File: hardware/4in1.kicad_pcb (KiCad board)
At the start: 6 copper layers, 41.6 x 42.5 mm, 222 parts, among them J1 SM08B-SRSS-TB, Q1 SP40N01GHNK, Q10 SP40N01GHNK, Q11 SP40N01GHNK, Q12 SP40N01GHNK, Q13 SP40N01GHNK, Q14 SP40N01GHNK, Q15 SP40N01GHNK, Q16 SP40N01GHNK, Q17 SP40N01GHNK, Q18 SP40N01GHNK, Q19 SP40N01GHNK, Q2 SP40N01GHNK, Q20 SP40N01GHNK, Q21 SP40N01GHNK, Q22 SP40N01GHNK, Q23 SP40N01GHNK, Q24 SP40N01GHNK, Q3 SP40N01GHNK, Q4 SP40N01GHNK, Q5 SP40N01GHNK, Q6 SP40N01GHNK, Q7 SP40N01GHNK, Q8 SP40N01GHNK, Q9 SP40N01GHNK, U10 NSG2065Q, U12 INA186A3IDCKR, U13 LMR54406DBVR, U14 FTC160808S4R7MBCA, U15 TLV76733DRVR, U2 AT32F421G8U7, U4 NSG2065Q, U5 AT32F421G8U7, U6 NSG2065Q, U7 AT32F421G8U7, U8 NSG2065Q, U9 AT32F421G8U7

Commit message: Rebrand back silkscreen to incutec, 4.7uF bulk caps on board
incutec silkscreen text added by Stan; bulk cap footprint fields
swapped to FH 1206B475K500NT 4.7uF 50V C29823 matching the committed
schematic change.

Co-Authored-By: Claude Fable 5 <noreply@anthropic.com>
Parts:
- C107 (x3), C108 (x3), C13 (x3), C14 (x3), C17, C18, C2 (x2), C26 (x3), C27 (x3), C3 (x2), C30, C43 (x3), C44 (x3), C6, C69, C70, C8, C82 (x3), C83 (x3), C84 (x3), C85 (x3), C9, C96, C97, C98, C99: value 10uF -> 4.7uF

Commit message: Sync silkscreen rev text to REV3.2 (pipeline rev sync)
Co-Authored-By: Claude Fable 5 <noreply@anthropic.com>
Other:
- board text added: "REV3.2"
- board text removed: "REV3.1"
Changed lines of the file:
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@@
 	)
 	(paper "A4")
+	(title_block
+		(rev "rev3.2")
+	)
 	(layers
 		(0 "F.Cu" signal)
@@
 		)
 	)
-	(gr_text "REV3.1"
+	(gr_text "REV3.2"
 		(at 87.12 56.53 0)
 		(layer "B.SilkS")
@@
 			(justify left bottom mirror)
 		)
-		(render_cache "REV3.1" 0
+		(render_cache "REV3.2" 0
 			(polygon
 				(pts
@@
 			(polygon
 				(pts
-					(xy 82.75759 56.224) (xy 83.052477 56.224) (xy 83.052477 54.604706) (xy 82.906297 54.458417) (xy 82.75759 54.458417)
+					(xy 83.059511 56.224) (xy 83.059511 55.441116) (xy 83.051258 55.374893) (xy 83.027065 55.316478)
+					(xy 82.986092 55.263832) (xy 82.933388 55.222921) (xy 82.874205 55.198631) (xy 82.80639 55.190303)
+					(xy 82.616357 55.190303) (xy 82.616357 54.753523) (xy 82.764624 54.753523) (xy 82.764624 55.043024)
+					(xy 83.059511 55.043024) (xy 83.059511 54.70934) (xy 83.051224 54.642106) (xy 83.027049 54.583432)
+					(xy 82.986311 54.531177) (xy 82.933733 54.490723) (xy 82.87462 54.46667) (xy 82.80683 54.458417)
+					(xy 82.574262 54.458417) (xy 82.50812 54.466599) (xy 82.449388 54.490636) (xy 82.396099 54.531397)
+					(xy 82.354516 54.583896) (xy 82.329898 54.642746) (xy 82.32147 54.710109) (xy 82.32147 55.236245)
+					(xy 82.329839 55.301929) (xy 82.354422 55.359974) (xy 82.396209 55.412429) (xy 82.44957 55.453182)
+					(xy 82.508411 55.477224) (xy 82.574701 55.485409) (xy 82.764624 55.485409) (xy 82.764624 55.928893)
+					(xy 82.616357 55.928893) (xy 82.616357 55.634886) (xy 82.32147 55.634886) (xy 82.32147 56.224)
 				)
 			)

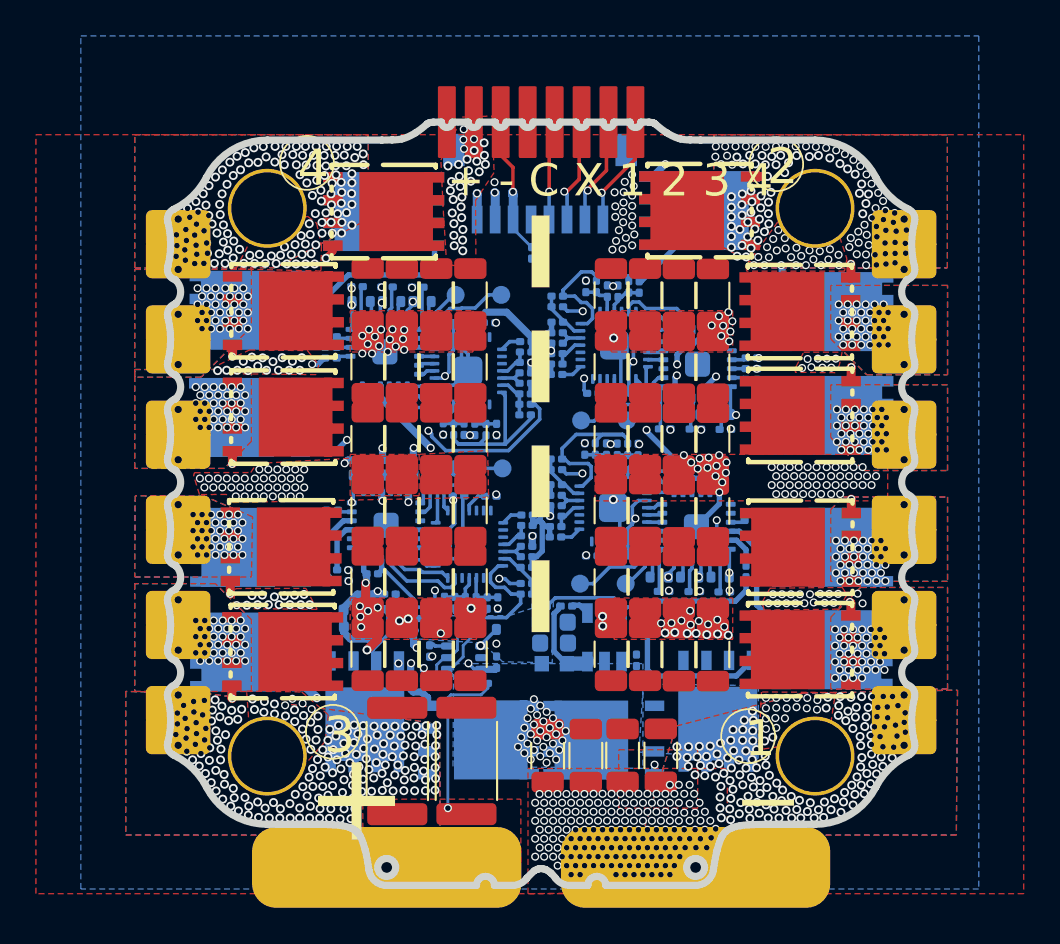
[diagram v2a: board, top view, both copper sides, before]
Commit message: Rebrand silkscreen to incutec, final rev3.3 pass (Stan)
Co-Authored-By: Claude Fable 5 <noreply@anthropic.com>
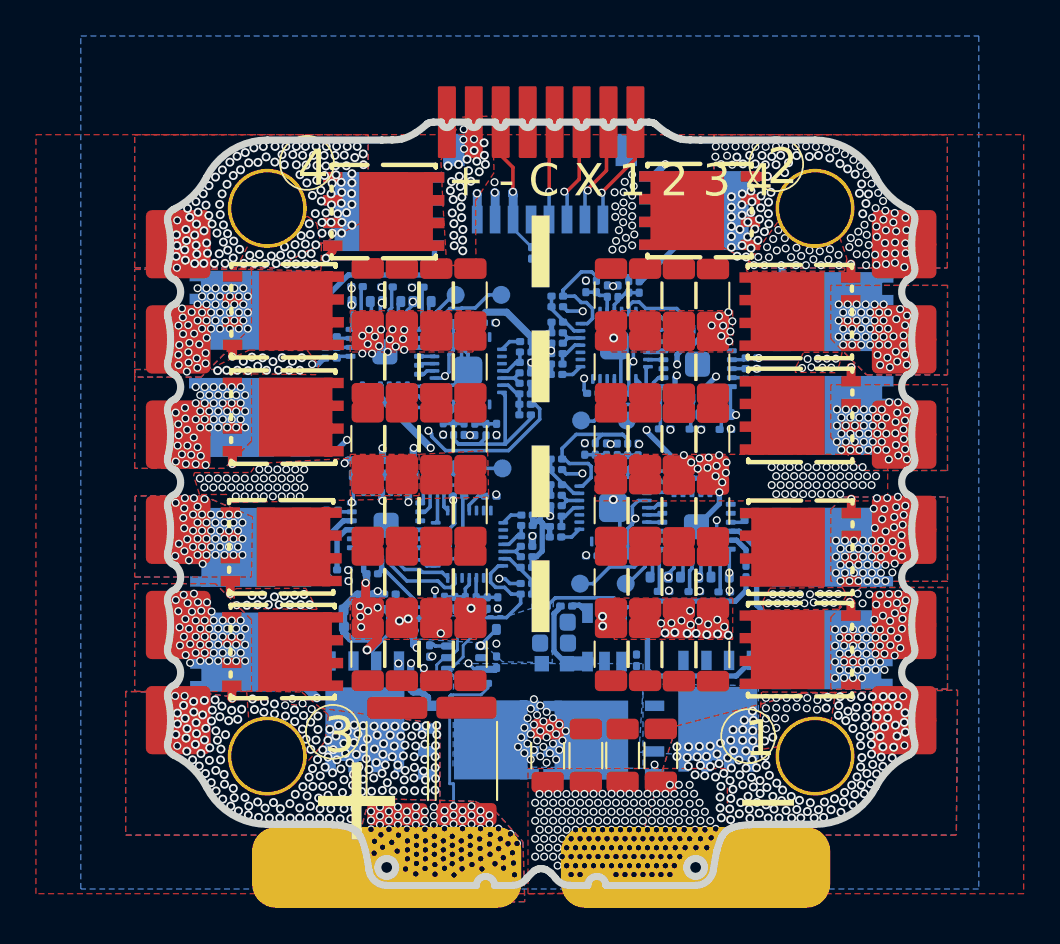
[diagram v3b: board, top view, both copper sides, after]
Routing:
- net /CSA+: vias 1 -> 102
- net /ESC4/MotorC: vias 38 -> 55
- net /ESC4/MotorB: vias 38 -> 58
- net /ESC4/MotorA: vias 110 -> 112
- net /ESC3/MotorC: vias 166 -> 169
- net /ESC3/MotorB: vias 38 -> 56
- net /ESC3/MotorA: vias 38 -> 52
- net /ESC2/MotorC: vias 108 -> 110
- net /ESC2/MotorB: vias 38 -> 53
- net /ESC2/MotorA: vias 38 -> 52
- net /ESC1/MotorC: vias 39 -> 60
- net /ESC1/MotorB: vias 42 -> 62
- net /ESC1/MotorA: vias 140 -> 142
- added copper zone on B.Cu, net /CSA+
- added copper zone on In1.Cu, net /CSA+
- added copper zone on In2.Cu, net /CSA+
- added copper zone on In3.Cu, net /CSA+
- added copper zone on In4.Cu, net /CSA+
